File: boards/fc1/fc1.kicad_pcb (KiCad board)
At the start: 4 copper layers, 39 x 39 mm, 36 parts, among them J1 USB_OTG, U1 MPU-9250, U2 DSC6001CI2A-016.0000T, U3 iCE40-LP8K-CM81, U4 AT25SF041-SSHD-B, U6 MIC5504-3.3YM5, U7 MIC5504-1.2YM5

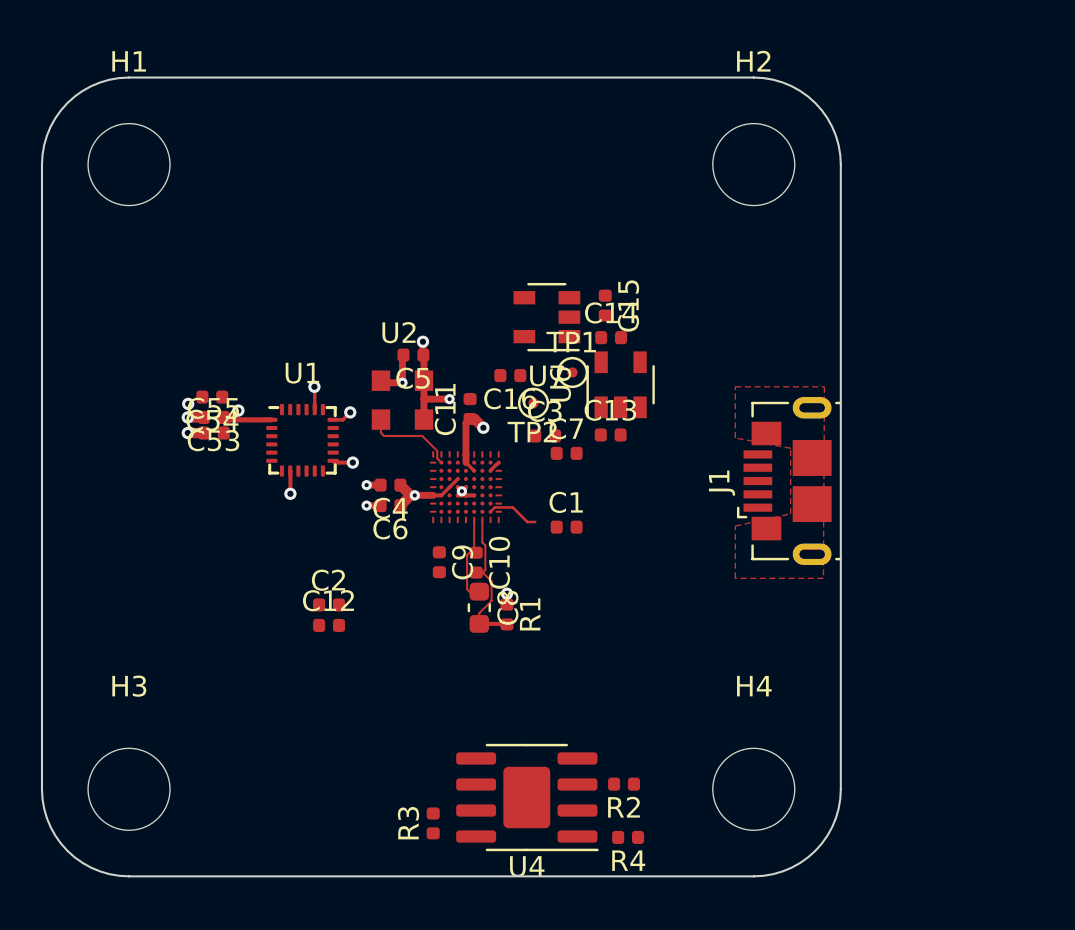
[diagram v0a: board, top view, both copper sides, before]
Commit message: More work to copy TinyFPGA schematic and layout
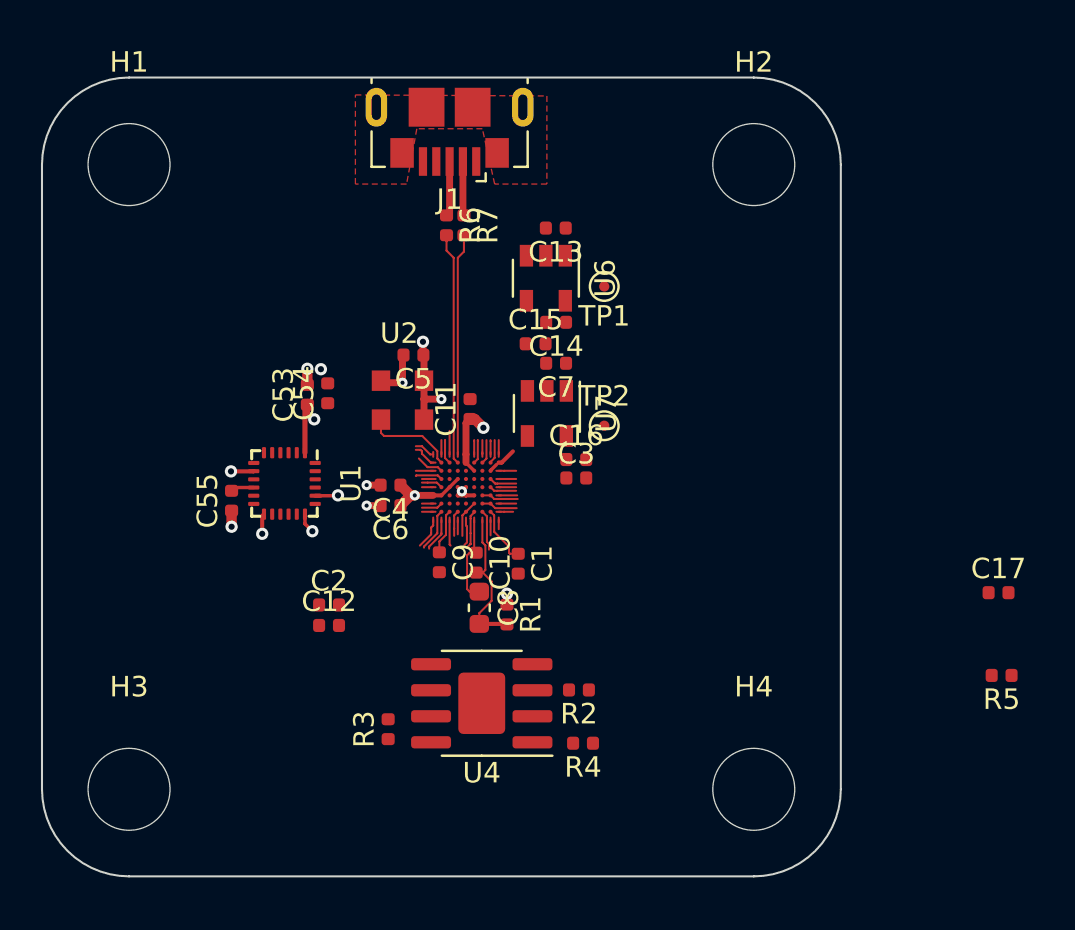
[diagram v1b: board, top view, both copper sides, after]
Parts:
- added C17: 10uF, Capacitor_SMD:C_0402_1005Metric, F.Cu at (146.7, 125.2)
- added R5: 1.5k, Resistor_SMD:R_0402_1005Metric, F.Cu at (146.8, 129.2)
- added R6: 68, Resistor_SMD:R_0402_1005Metric, F.Cu at (119.8, 107.2)
- added R7: 68, Resistor_SMD:R_0402_1005Metric, F.Cu at (120.6, 107.2)
- moved J1 23.7 mm to (119.9, 102.7), turned to 180 degrees
- moved C13 10.4 mm to (125.1, 107.3), turned to 180 degrees
- moved U6 6.35 mm to (124.6, 109.8), turned to 270 degrees
- moved C54 5.64 mm to (114.0, 115.4), turned to 90 degrees
- moved C16 5.21 mm to (126.1, 118.7), turned to 0 degrees
- moved R4 5.10 mm to (126.4, 132.5)
- moved U4 5.10 mm to (121.5, 130.6)
- moved R2 5.10 mm to (126.2, 129.9)
- moved R3 5.10 mm to (116.9, 131.8)
- moved U7 4.70 mm to (124.7, 116.4), turned to 270 degrees
- moved C53 4.70 mm to (113.0, 115.5), turned to 90 degrees
- moved TP1 4.48 mm to (127.5, 110.2), turned to 180 degrees
- moved C7 4.43 mm to (125.1, 114.0), turned to 180 degrees
- moved C15 3.88 mm to (124.1, 113.0), turned to 0 degrees
- moved TP2 3.62 mm to (127.5, 117.0), turned to 0 degrees
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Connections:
- J1 pad 5: Net-(J1-Pad5) -> GND
- J1 pad 6: Net-(J1-Pad6) -> GND
- U3 pad A3: Net-(U3-PadA3) -> USB_PU
- U3 pad A4: Net-(U3-PadA4) -> USB_N
- U3 pad B4: Net-(U3-PadB4) -> USB_P
- U3 pad F8: Net-(U3-PadF8) -> FLASH_CS
- U3 pad G8: Net-(U3-PadG8) -> FLASH_SCLK
- U3 pad H5: Net-(U3-PadH5) -> FLASH_MOSI
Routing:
- net USB_P: track 0.00 -> 11.6 mm
- net USB_N: track 0.00 -> 10.8 mm
- net +3V3: track 17.5 -> 21.6 mm
- net Net-(J1-Pad3): track 0.00 -> 2.69 mm
- net Net-(J1-Pad2): track 0.00 -> 2.64 mm
- net Net-(U3-PadH2): track 0.00 -> 2.10 mm
- net FLASH_MISO: track 0.00 -> 1.98 mm
- net Net-(U3-PadH6): track 0.00 -> 1.89 mm
- net FLASH_MOSI: track 0.00 -> 1.81 mm
- net FLASH_CS: track 0.00 -> 1.80 mm
- net FLASH_SCLK: track 0.00 -> 1.77 mm
- net Net-(U3-PadJ2): track 0.00 -> 1.65 mm
- net Net-(U3-PadJ1): track 0.00 -> 1.52 mm
- net Net-(U3-PadC2): track 0.00 -> 1.35 mm
- net Net-(U3-PadD8): track 0.00 -> 1.34 mm
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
